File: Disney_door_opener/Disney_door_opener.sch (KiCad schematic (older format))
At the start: 29 parts, among them J1 Screw_Terminal_01x02, J2 Conn_01x02, J3 Conn_01x02, J4 Conn_01x05, J5 Screw_Terminal_01x02, U1 LM2596S-5, U2 ESP32_DevKit_V1_DOIT, U3 MAX98357A

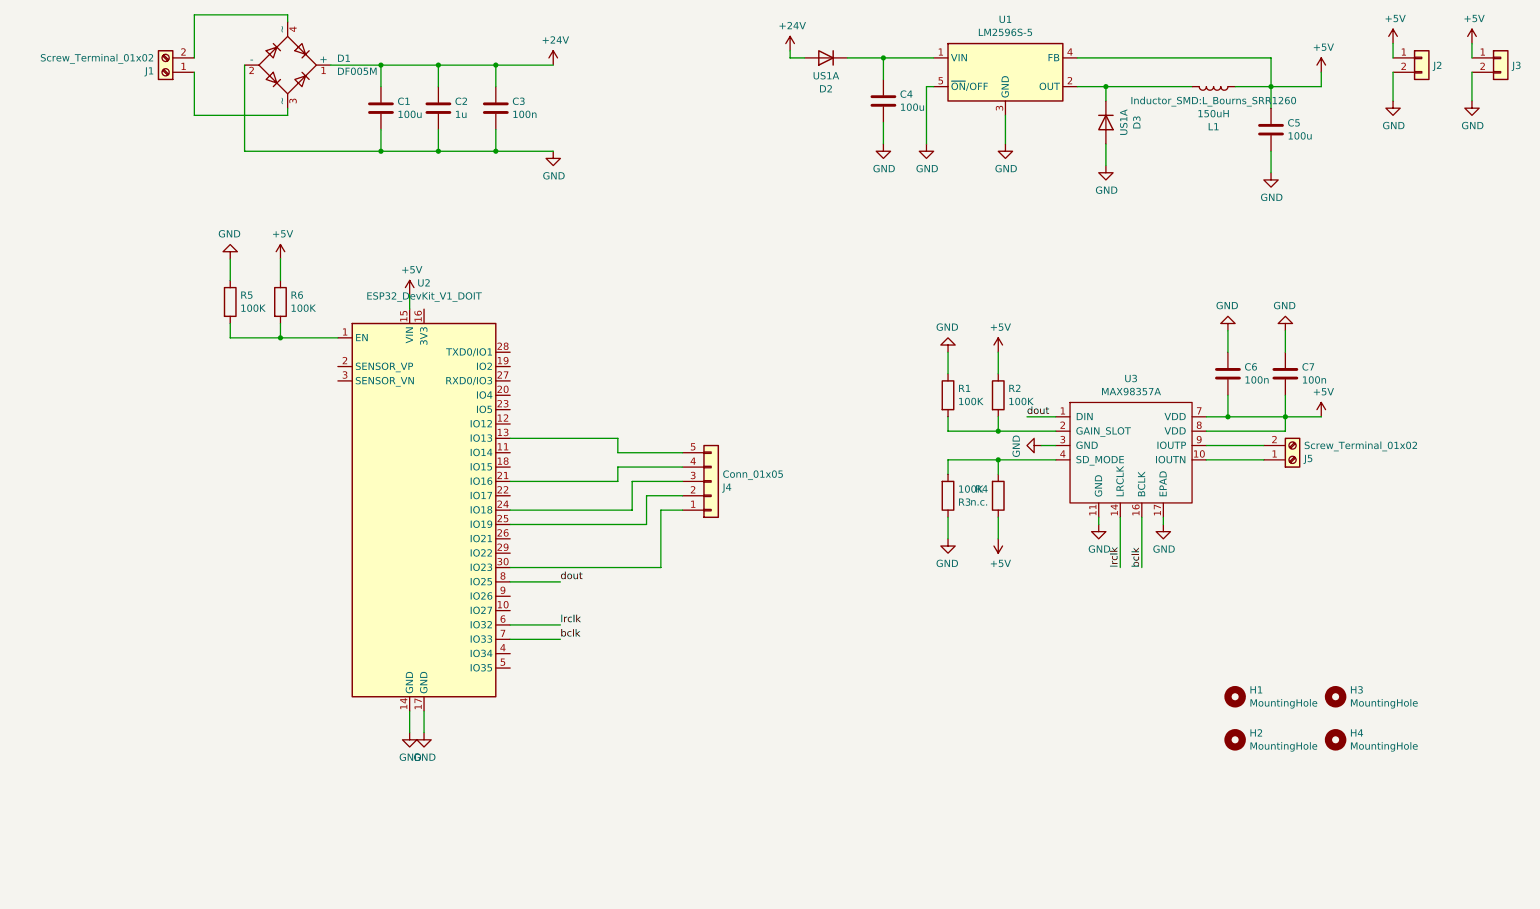
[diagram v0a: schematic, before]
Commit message: Changed esp32 board with 2 pinheader connectors. Updated resistor values for proper operation.
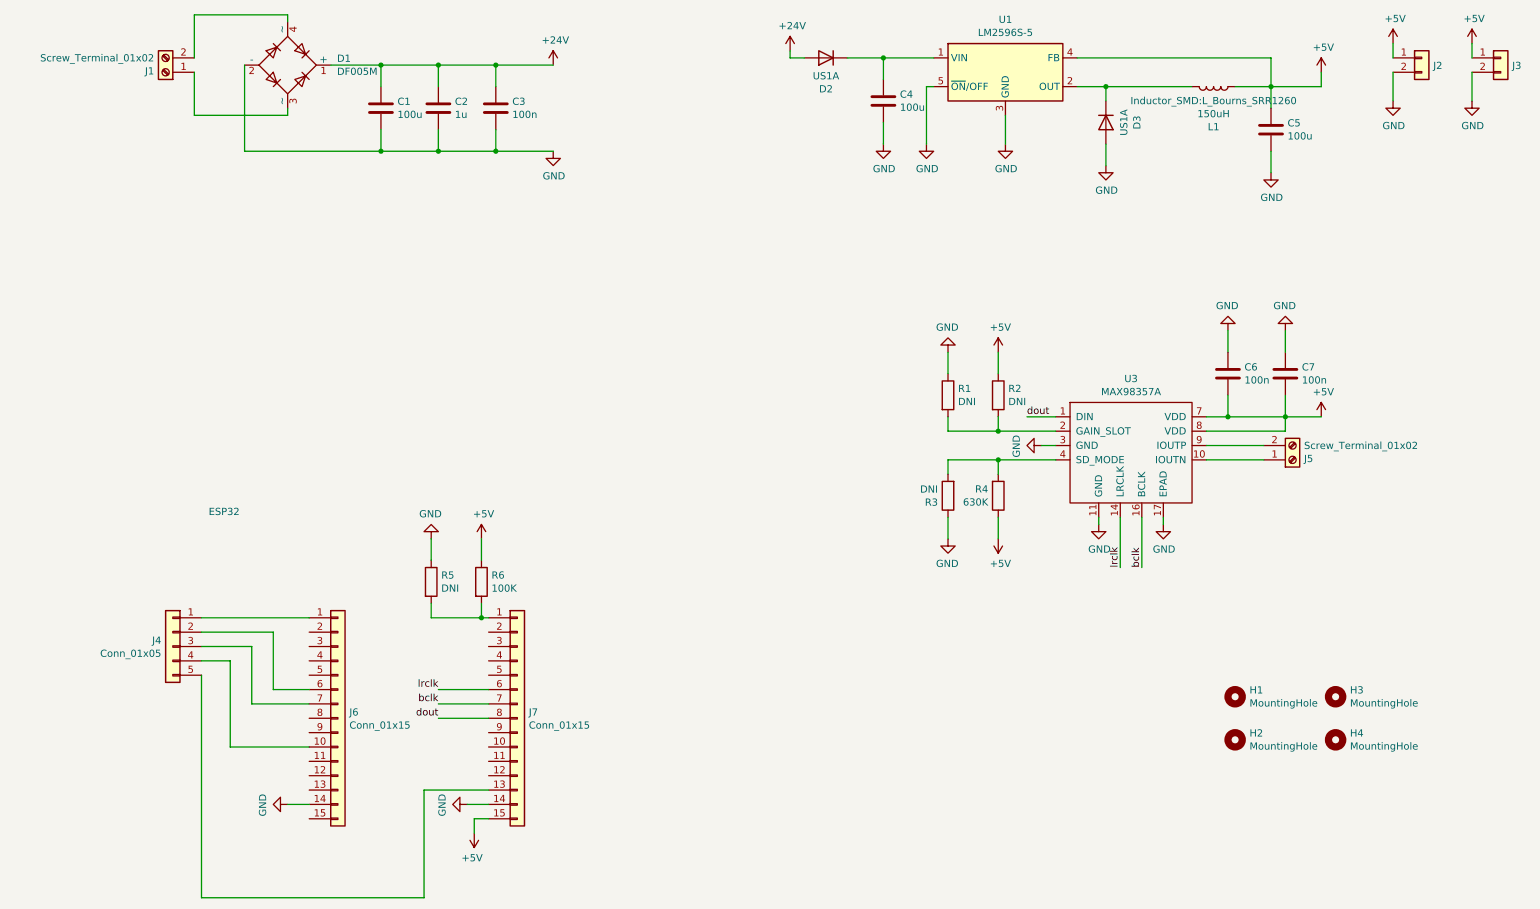
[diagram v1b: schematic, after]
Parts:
- removed U2: ESP32_DevKit_V1_DOIT, Disney_door_opener:esp32_devkit_v1_doit, symbol New_Library:ESP32_DevKit_V1_DOIT
- added J6, J7: Conn_01x15, Connector_PinHeader_2.54mm:PinHeader_1x15_P2.54mm_Vertical, symbol Connector_Generic:Conn_01x15
- R1, R2, R3, R5: value 100K -> DNI
- R4: value n.c. -> 630K
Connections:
- net +5V: now also J7.15 (Pin_15)
- net GND: now also J6.14 (Pin_14), J7.14 (Pin_14)
- net bclk: now also J7.7 (Pin_7)
- net dout: now also J7.8 (Pin_8)
- net lrclk: now also J7.6 (Pin_6)
- net at R5.2, R6.2: now also J7.1 (Pin_1)
- net at J4.5 (Pin_5): now also J7.13 (Pin_13)
- net at J4.4 (Pin_4): now also J6.10 (Pin_10)
- net at J4.3 (Pin_3): now also J6.7 (Pin_7)
- net at J4.2 (Pin_2): now also J6.6 (Pin_6)
- net at J4.1 (Pin_1): now also J6.1 (Pin_1)
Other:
- note added: "ESP32\n"
- moved on the sheet: J4, R5, R6
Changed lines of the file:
@@
-$EndComp
-$Comp
-L New_Library:ESP32_DevKit_V1_DOIT U2
-U 1 1 646EB8FE
-P 3300 4250
-F 0 "U2" H 3300 5831 50  0000 C CNN
-F 1 "ESP32_DevKit_V1_DOIT" H 3300 5740 50  0000 C CNN
-F 2 "Disney_door_opener:esp32_devkit_v1_doit" H 2850 5600 50  0001 C CNN
-F 3 "https://aliexpress.com/item/32864722159.html" H 2850 5600 50  0001 C CNN
-	1    3300 4250
-	1    0    0    -1
 $EndComp
 $Comp
@@
 $EndComp
 $Comp
-L Connector_Generic:Conn_01x05 J4
-U 1 1 646F431E
-P 5300 4050
-F 0 "J4" H 5380 4092 50  0000 L CNN
-F 1 "Conn_01x05" H 5380 4001 50  0000 L CNN
-F 2 "Connector_PinHeader_2.54mm:PinHeader_1x05_P2.54mm_Vertical" H 5300 4050 50  0001 C CNN
-F 3 "~" H 5300 4050 50  0001 C CNN
-	1    5300 4050
-	1    0    0    1
-$EndComp
-Wire Wire Line
-	3900 3750 4650 3750
-Wire Wire Line
-	3900 4250 4750 4250
-Wire Wire Line
-	4750 4250 4750 4050
-Wire Wire Line
-	3900 4350 4850 4350
-Wire Wire Line
-	4850 4350 4850 4150
-Wire Wire Line
-	3900 4650 4950 4650
-Wire Wire Line
-	4650 4050 4650 3950
-Wire Wire Line
-	3900 4050 4650 4050
-Wire Wire Line
-	4650 3850 4650 3750
-$Comp
 L New_Library:MAX98357A U3
 U 1 1 64707385
@@
 	7700 3800 7600 3800
 Wire Wire Line
-	3900 5050 4250 5050
-Text Label 4250 5050 0    50   ~ 0
-lrclk
-Wire Wire Line
 	8150 4300 8150 4650
 Text Label 8150 4650 1    50   ~ 0
@@
 Text Label 8300 4650 1    50   ~ 0
 bclk
-Wire Wire Line
-	3900 5150 4250 5150
-Text Label 4250 5150 0    50   ~ 0
-bclk
-Wire Wire Line
-	3900 4750 4250 4750
-Text Label 4250 4750 0    50   ~ 0
-dout
 Wire Wire Line
 	7700 3600 7500 3600
@@
 P 7300 3450
 F 0 "R2" H 7370 3496 50  0000 L CNN
-F 1 "100K" H 7370 3405 50  0000 L CNN
+F 1 "DNI" H 7370 3405 50  0000 L CNN
 F 2 "Resistor_SMD:R_1206_3216Metric_Pad1.30x1.75mm_HandSolder" V 7230 3450 50  0001 C CNN
 F 3 "~" H 7300 3450 50  0001 C CNN
@@
 P 6950 3450
 F 0 "R1" H 7020 3496 50  0000 L CNN
-F 1 "100K" H 7020 3405 50  0000 L CNN
+F 1 "DNI" H 7020 3405 50  0000 L CNN
 F 2 "Resistor_SMD:R_1206_3216Metric_Pad1.30x1.75mm_HandSolder" V 6880 3450 50  0001 C CNN
 F 3 "~" H 6950 3450 50  0001 C CNN
@@
 P 7300 4150
 F 0 "R4" H 7230 4104 50  0000 R CNN
-F 1 "n.c." H 7230 4195 50  0000 R CNN
+F 1 "630K" H 7230 4195 50  0000 R CNN
 F 2 "Resistor_SMD:R_1206_3216Metric_Pad1.30x1.75mm_HandSolder" V 7230 4150 50  0001 C CNN
 F 3 "~" H 7300 4150 50  0001 C CNN
 	1    7300 4150
-	1    0    0    1
-$EndComp
-$Comp
-L Device:R R3
-U 1 1 6474CBF2
-P 6950 4150
-F 0 "R3" H 7020 4196 50  0000 L CNN
-F 1 "100K" H 7020 4105 50  0000 L CNN
-F 2 "Resistor_SMD:R_1206_3216Metric_Pad1.30x1.75mm_HandSolder" V 6880 4150 50  0001 C CNN
-F 3 "~" H 6950 4150 50  0001 C CNN
-	1    6950 4150
 	1    0    0    1
 $EndComp
@@
 	-1   0    0    1
 $EndComp
-Wire Wire Line
-	4950 4650 4950 4250
-Wire Wire Line
-	4950 4250 5100 4250
-Wire Wire Line
-	4850 4150 5100 4150
-Wire Wire Line
-	4750 4050 5100 4050
-Wire Wire Line
-	4650 3950 5100 3950
-Wire Wire Line
-	5100 3850 4650 3850
-Wire Wire Line
-	3200 5650 3200 5800
-$Comp
-L power:GND #PWR0124
-U 1 1 646F4E1A
-P 3200 5800
-F 0 "#PWR0124" H 3200 5550 50  0001 C CNN
-F 1 "GND" H 3205 5627 50  0000 C CNN
-F 2 "" H 3200 5800 50  0001 C CNN
-F 3 "" H 3200 5800 50  0001 C CNN
-	1    3200 5800
-	1    0    0    -1
-$EndComp
-Wire Wire Line
-	3300 5650 3300 5800
-$Comp
-L power:GND #PWR0125
-U 1 1 646F715B
-P 3300 5800
-F 0 "#PWR0125" H 3300 5550 50  0001 C CNN
-F 1 "GND" H 3305 5627 50  0000 C CNN
-F 2 "" H 3300 5800 50  0001 C CNN
-F 3 "" H 3300 5800 50  0001 C CNN
-	1    3300 5800
-	1    0    0    -1
-$EndComp
-$Comp
-L power:+5V #PWR0126
-U 1 1 646F9A11
-P 3200 2750
-F 0 "#PWR0126" H 3200 2600 50  0001 C CNN
-F 1 "+5V" H 3215 2923 50  0000 C CNN
-F 2 "" H 3200 2750 50  0001 C CNN
-F 3 "" H 3200 2750 50  0001 C CNN
-	1    3200 2750
-	1    0    0    -1
-$EndComp
-Wire Wire Line
-	3200 2850 3200 2750
-$Comp
-L Device:R R6
-U 1 1 64741E4C
-P 2300 2800
-F 0 "R6" H 2370 2846 50  0000 L CNN
-F 1 "100K" H 2370 2755 50  0000 L CNN
-F 2 "Resistor_SMD:R_1206_3216Metric_Pad1.30x1.75mm_HandSolder" V 2230 2800 50  0001 C CNN
-F 3 "~" H 2300 2800 50  0001 C CNN
-	1    2300 2800
-	1    0    0    -1
-$EndComp
-$Comp
-L Device:R R5
-U 1 1 64741E52
-P 1950 2800
-F 0 "R5" H 2020 2846 50  0000 L CNN
-F 1 "100K" H 2020 2755 50  0000 L CNN
-F 2 "Resistor_SMD:R_1206_3216Metric_Pad1.30x1.75mm_HandSolder" V 1880 2800 50  0001 C CNN
-F 3 "~" H 1950 2800 50  0001 C CNN
-	1    1950 2800
-	1    0    0    -1
-$EndComp
-Wire Wire Line
-	2700 3050 2300 3050
-Wire Wire Line
-	2300 3050 2300 2950
-Wire Wire Line
-	2300 3050 1950 3050
-Wire Wire Line
-	1950 3050 1950 2950
-Connection ~ 2300 3050
-$Comp
-L power:+5V #PWR0127
-U 1 1 64741E5D
-P 2300 2500
-F 0 "#PWR0127" H 2300 2350 50  0001 C CNN
-F 1 "+5V" H 2315 2673 50  0000 C CNN
-F 2 "" H 2300 2500 50  0001 C CNN
-F 3 "" H 2300 2500 50  0001 C CNN
-	1    2300 2500
-	1    0    0    -1
-$EndComp
-$Comp
-L power:GND #PWR0128
-U 1 1 64741E63
-P 1950 2500
-F 0 "#PWR0128" H 1950 2250 50  0001 C CNN
-F 1 "GND" H 1955 2327 50  0000 C CNN
-F 2 "" H 1950 2500 50  0001 C CNN
-F 3 "" H 1950 2500 50  0001 C CNN
-	1    1950 2500
-	-1   0    0    1
-$EndComp
-Wire Wire Line
-	1950 2500 1950 2650
-Wire Wire Line
-	2300 2650 2300 2500
 $Comp
 L Mechanical:MountingHole H3
@@
 	1    0    0    -1
 $EndComp
+$Comp
+L Connector_Generic:Conn_01x15 J6
+U 1 1 6485E55E
+P 2700 5700
+F 0 "J6" H 2780 5742 50  0000 L CNN
+F 1 "Conn_01x15" H 2780 5651 50  0000 L CNN
+F 2 "Connector_PinHeader_2.54mm:PinHeader_1x15_P2.54mm_Vertical" H 2700 5700 50  0001 C CNN
+F 3 "~" H 2700 5700 50  0001 C CNN
+	1    2700 5700
+	1    0    0    -1
+$EndComp
+$Comp
+L Connector_Generic:Conn_01x15 J7
+U 1 1 6487741E
+P 3950 5700
+F 0 "J7" H 4030 5742 50  0000 L CNN
+F 1 "Conn_01x15" H 4030 5651 50  0000 L CNN
+F 2 "Connector_PinHeader_2.54mm:PinHeader_1x15_P2.54mm_Vertical" H 3950 5700 50  0001 C CNN
+F 3 "~" H 3950 5700 50  0001 C CNN
+	1    3950 5700
+	1    0    0    -1
+$EndComp
+Wire Wire Line
+	3750 5000 3700 5000
+Wire Wire Line
+	3750 5500 3400 5500
+Text Label 3400 5500 2    50   ~ 0
+lrclk
+Wire Wire Line
+	3750 5600 3400 5600
+Text Label 3400 5600 2    50   ~ 0
+bclk
+Text Label 3400 5700 2    50   ~ 0
+dout
+Wire Wire Line
+	3750 5700 3400 5700
+Wire Wire Line
+	3750 6200 3300 6200
+Wire Wire Line
+	3300 6200 3300 6950
+Wire Wire Line
+	3650 6400 3650 6500
+$Comp
+L power:+5V #PWR0129
+U 1 1 648ADAEA
+P 3650 6500
+F 0 "#PWR0129" H 3650 6350 50  0001 C CNN
+F 1 "+5V" H 3665 6673 50  0000 C CNN
+F 2 "" H 3650 6500 50  0001 C CNN
+F 3 "" H 3650 6500 50  0001 C CNN
+	1    3650 6500
+	-1   0    0    1
+$EndComp
+Wire Wire Line
+	3750 6400 3650 6400
+Wire Wire Line
+	3750 6300 3600 6300
+$Comp
+L power:GND #PWR0124
+U 1 1 648B90AC
+P 3600 6300
+F 0 "#PWR0124" H 3600 6050 50  0001 C CNN
+F 1 "GND" H 3605 6127 50  0000 C CNN
+F 2 "" H 3600 6300 50  0001 C CNN
+F 3 "" H 3600 6300 50  0001 C CNN
+	1    3600 6300
+	0    1    1    0
+$EndComp
+Wire Wire Line
+	2500 6300 2350 6300
+$Comp
+L power:GND #PWR0125
+U 1 1 648BD950
+P 2350 6300
+F 0 "#PWR0125" H 2350 6050 50  0001 C CNN
+F 1 "GND" H 2355 6127 50  0000 C CNN
+F 2 "" H 2350 6300 50  0001 C CNN
+F 3 "" H 2350 6300 50  0001 C CNN
+	1    2350 6300
+	0    1    1    0
+$EndComp
+Wire Wire Line
+	3700 4600 3700 4450
+Wire Wire Line
+	3350 4450 3350 4600
+$Comp
+L power:GND #PWR0128
+U 1 1 64741E63
+P 3350 4450
+F 0 "#PWR0128" H 3350 4200 50  0001 C CNN
+F 1 "GND" H 3355 4277 50  0000 C CNN
+F 2 "" H 3350 4450 50  0001 C CNN
+F 3 "" H 3350 4450 50  0001 C CNN
+	1    3350 4450
+	-1   0    0    1
+$EndComp
+$Comp
+L power:+5V #PWR0127
+U 1 1 64741E5D
+P 3700 4450
+F 0 "#PWR0127" H 3700 4300 50  0001 C CNN
+F 1 "+5V" H 3715 4623 50  0000 C CNN
+F 2 "" H 3700 4450 50  0001 C CNN
+F 3 "" H 3700 4450 50  0001 C CNN
+	1    3700 4450
+	1    0    0    -1
+$EndComp
+Wire Wire Line
+	3350 5000 3350 4900
+Wire Wire Line
+	3700 5000 3350 5000
+Wire Wire Line
+	3700 5000 3700 4900
+$Comp
+L Device:R R5
+U 1 1 64741E52
+P 3350 4750
+F 0 "R5" H 3420 4796 50  0000 L CNN
+F 1 "DNI" H 3420 4705 50  0000 L CNN
+F 2 "Resistor_SMD:R_1206_3216Metric_Pad1.30x1.75mm_HandSolder" V 3280 4750 50  0001 C CNN
+F 3 "~" H 3350 4750 50  0001 C CNN
+	1    3350 4750
+	1    0    0    -1
+$EndComp
+$Comp
+L Device:R R6
+U 1 1 64741E4C
+P 3700 4750
+F 0 "R6" H 3770 4796 50  0000 L CNN
+F 1 "100K" H 3770 4705 50  0000 L CNN
+F 2 "Resistor_SMD:R_1206_3216Metric_Pad1.30x1.75mm_HandSolder" V 3630 4750 50  0001 C CNN
+F 3 "~" H 3700 4750 50  0001 C CNN
+	1    3700 4750
+	1    0    0    -1
+$EndComp
+Connection ~ 3700 5000
+$Comp
+L Connector_Generic:Conn_01x05 J4
+U 1 1 646F431E
+P 1550 5200
+F 0 "J4" H 1630 5242 50  0000 L CNN
+F 1 "Conn_01x05" H 1630 5151 50  0000 L CNN
+F 2 "Connector_PinHeader_2.54mm:PinHeader_1x05_P2.54mm_Vertical" H 1550 5200 50  0001 C CNN
+F 3 "~" H 1550 5200 50  0001 C CNN
+	1    1550 5200
+	-1   0    0    -1
+$EndComp
+Wire Wire Line
+	1750 5000 2500 5000
+Wire Wire Line
+	2250 5500 2250 5100
+Wire Wire Line
+	2250 5100 1750 5100
+Wire Wire Line
+	2250 5500 2500 5500
+Wire Wire Line
+	2100 5600 2100 5200
+Wire Wire Line
+	2100 5200 1750 5200
+Wire Wire Line
+	1950 5900 1950 5300
+Wire Wire Line
+	1950 5300 1750 5300
+Wire Wire Line
+	2100 5600 2500 5600
+Wire Wire Line
+	1950 5900 2500 5900
+Wire Wire Line
+	1750 6950 1750 5400
+Wire Wire Line
+	1750 6950 3300 6950
+Text Notes 1800 4300 0    50   ~ 0
+ESP32\n
+$Comp
+L Device:R R3
+U 1 1 6474CBF2
+P 6950 4150
+F 0 "R3" H 7020 4196 50  0000 L CNN
+F 1 "DNI" H 7020 4105 50  0000 L CNN
+F 2 "Resistor_SMD:R_1206_3216Metric_Pad1.30x1.75mm_HandSolder" V 6880 4150 50  0001 C CNN
+F 3 "~" H 6950 4150 50  0001 C CNN
+	1    6950 4150
+	-1   0    0    1
+$EndComp
 $EndSCHEMATC
